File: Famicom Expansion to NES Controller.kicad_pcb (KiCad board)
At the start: 2 copper layers, 63.1 x 24.9 mm, 7 parts, among them J1 DB15_Female, J2 Conn_01x07_Female, J3 Conn_01x07_Female

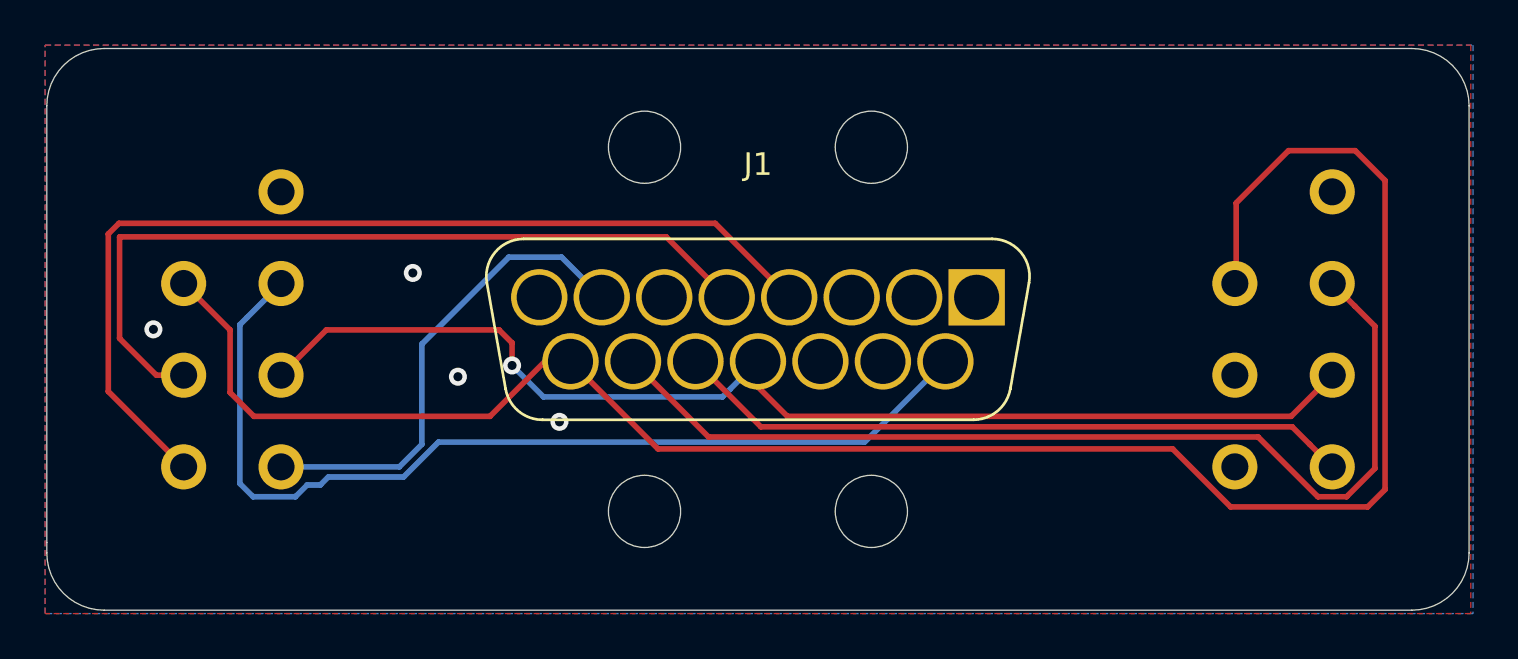
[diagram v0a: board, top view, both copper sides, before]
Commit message: Added HDMI Ports for Blissbox compatibility
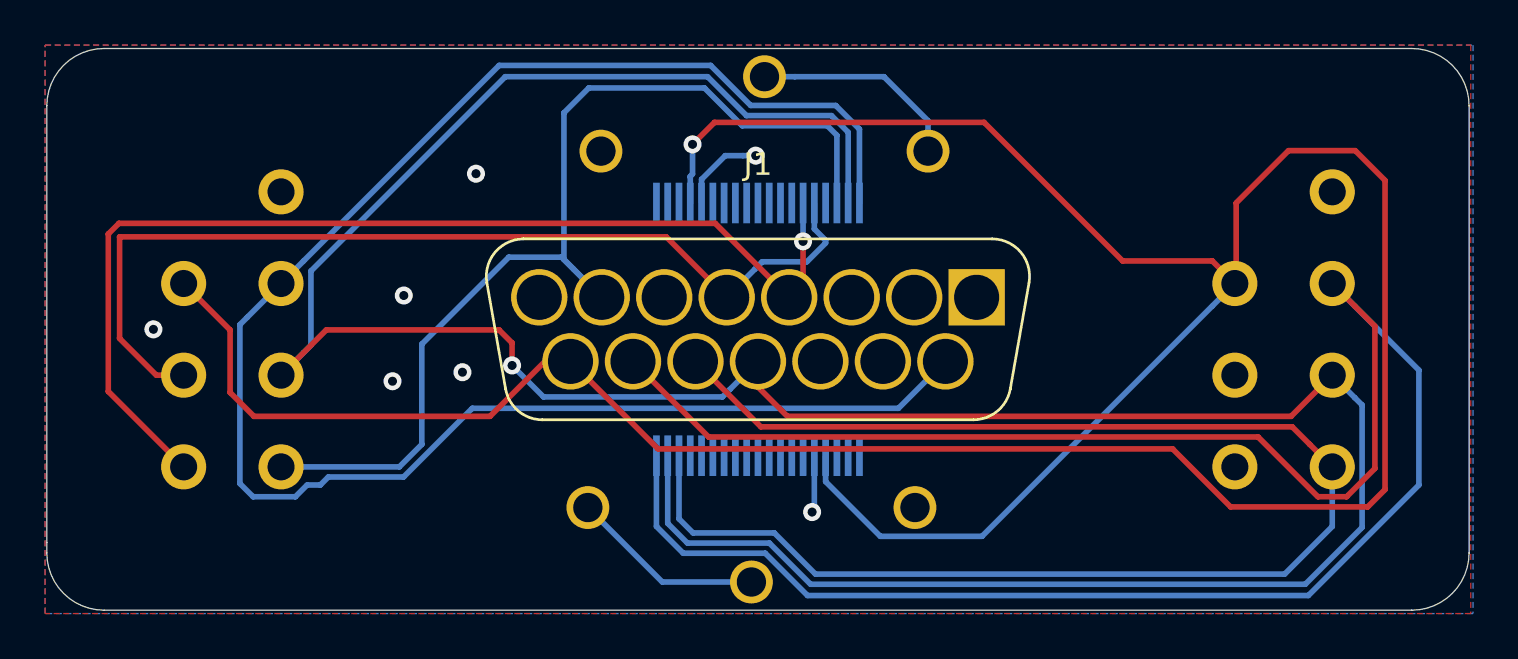
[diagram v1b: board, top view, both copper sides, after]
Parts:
- removed  : , MountingHole:MountingHole_3.2mm_M3 (x4)
- added J4: HDMI_A, Tinkerplunk:HDMI_VERT_47659-1000, B.Cu at (155.0, 68.1)
- added J5: HDMI_A, Tinkerplunk:HDMI_VERT_47659-1000, B.Cu at (155.0, 56.9)
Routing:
- net LATCH: track 52.3 -> 132.3 mm
- net +5V: track 86.7 -> 141.7 mm, vias 0 -> 1
- net CLOCK(1): track 44.9 -> 95.6 mm
- net DATA(1): track 30.2 -> 66.8 mm
- net CLOCK(2): track 43.6 -> 77.7 mm
- net DATA(2): track 21.4 -> 46.7 mm
- net GND: track 0.00 -> 24.4 mm, vias 4 -> 7
- net D3: track 36.0 -> 43.4 mm
- net D4: track 43.4 -> 47.9 mm, vias 0 -> 1

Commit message: not sure what changes I made
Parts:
- added REF**: , MountingHole:MountingHole_3.2mm_M3, F.Cu at (166.2, 70.7)
- added REF**: , MountingHole:MountingHole_3.2mm_M3, F.Cu at (143.8, 54.3)
- added REF**: , MountingHole:MountingHole_3.2mm_M3, F.Cu at (143.8, 70.7)
- added REF**: , MountingHole:MountingHole_3.2mm_M3, F.Cu at (166.2, 54.3)
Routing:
- net DATA(2): track 46.7 -> 37.9 mm
- net +5V: track 141.7 -> 150.4 mm
- net LATCH: track 132.3 -> 128.3 mm
- net D3: track 43.4 -> 39.9 mm
- net DATA(1): track 66.8 -> 64.8 mm
- net CLOCK(2): track 77.7 -> 76.6 mm
- net D4: track 47.9 -> 46.8 mm
- net GND: track 24.4 -> 25.0 mm, vias 7 -> 10
